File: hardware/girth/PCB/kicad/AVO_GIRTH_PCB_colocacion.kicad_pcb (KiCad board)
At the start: 4 copper layers, 65.5 x 43.5 mm, 115 parts, among them J1 USB-C 16P, J2 BATERÍA 1S, K1 G6KU-2F-Y DC3, Q1 AO3401A, Q10 AO3401A, Q11 AO3400A, Q12 2N7002, Q13 AO3400A, Q14 AO3401A, Q15 2N7002, Q16 2N7002, Q2 AO3401A, Q3 AO3401A, SW1 REED (1), SW2 REED (2), U1 BQ51013BRHLR, U2 BQ24072RGTR, U3 RT9080-33GJ5, U4 ESP32-C6-MINI-1U-N4, U5 BNO085, U6 USBLC6-2SC6, Y1 32,768 kHz 12,5 pF

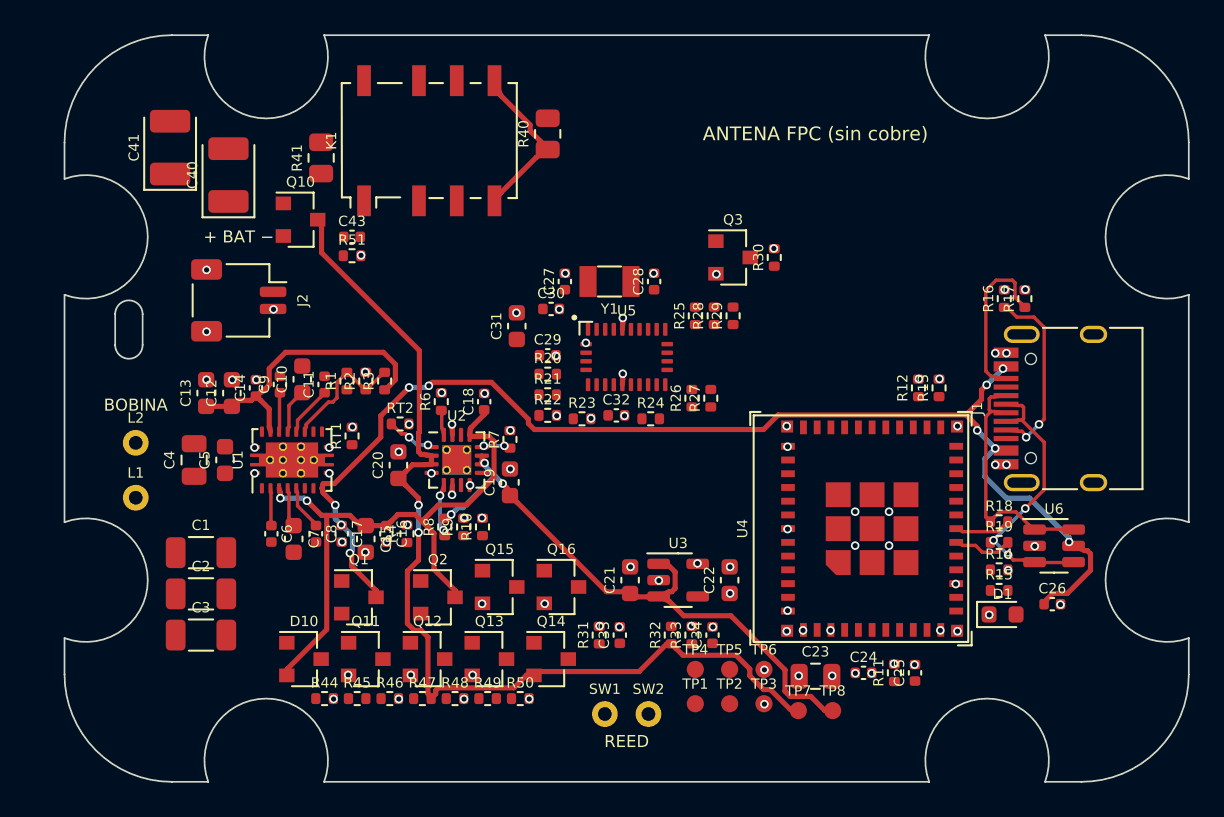
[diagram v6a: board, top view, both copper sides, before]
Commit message: PCB cincha: relé también se cierra desde el ESP32 (GPIO14), puerta de fabricación en CI, reparación de ruteado
- Relé: camino SET por firmware (Q17/Q18/D11/R52–R55): con la base puesta el ESP32 vive del camino de potencia del
  cargador y puede volver a cerrar el relé → el sistema nunca queda bloqueado apagado.
- GND de las QFN unidos a su pad térmico por pistas cortas (sin vías que tapen la salida de los pines vecinos).
- Referencias en la capa Fab; huellas enlazadas a los símbolos (DRC con paridad de esquema).
- CI: puerta bloqueante (0 errores DRC, 0 incompletas, 0 paridad, ERC limpio); ficheros FINAL solo si pasa; rojo si no.
- fuente/repair.py: completa las conexiones que deja Freerouting y genera la placa ruteada que usa el CI.

Co-Authored-By: Claude Opus 5.5 <noreply@anthropic.com>
Claude-Session: https://claude.ai/code/session_01CHDvF8BfHwPLkrFs9S3ECm
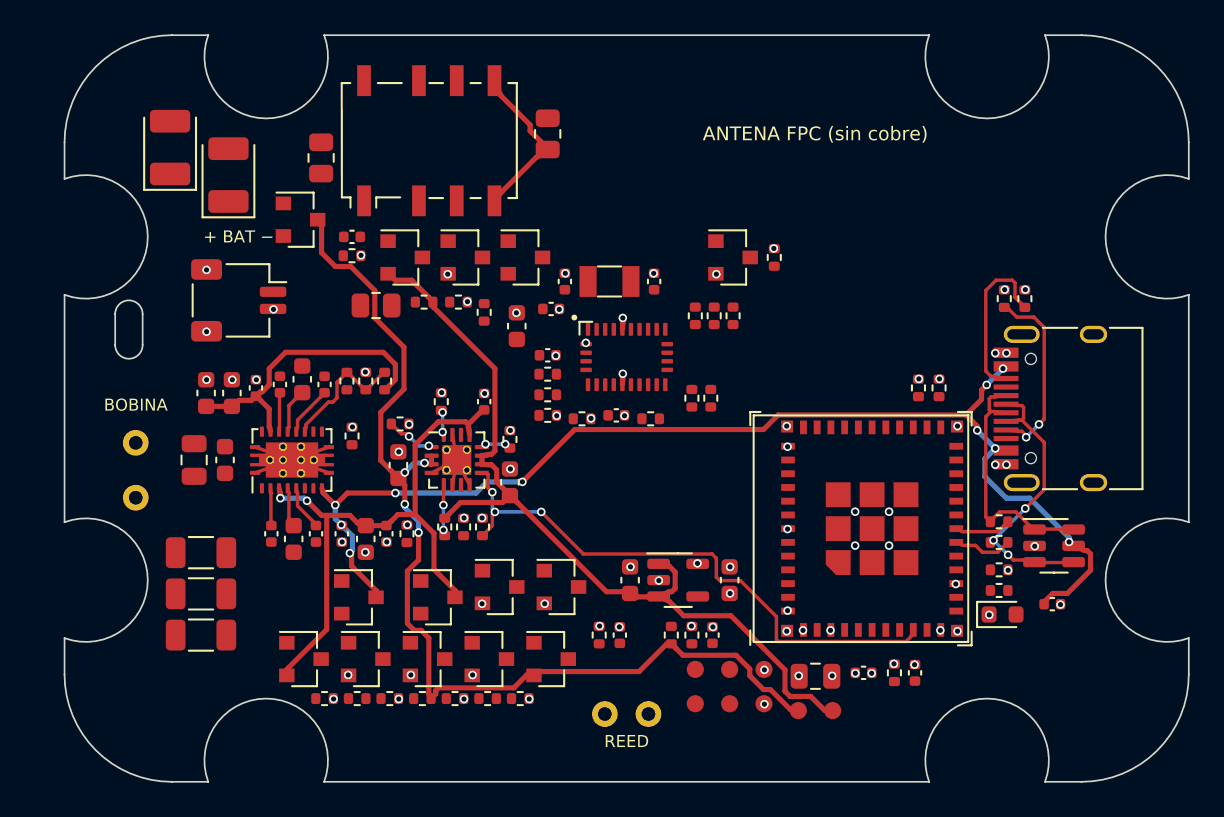
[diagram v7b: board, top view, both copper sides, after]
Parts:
- added D11: BAT54C, AVO:SOT-23, F.Cu at (94.1, 91.2)
- added Q17: AO3401A, AVO:SOT-23, F.Cu at (87.1, 91.2)
- added Q18: 2N7002, AVO:SOT-23, F.Cu at (90.6, 91.2)
- added R52: 10R, AVO:R_0805_2012Metric, F.Cu at (85.4, 94.0)
- added R53: 100k, AVO:R_0402_1005Metric, F.Cu at (88.2, 93.8)
- added R54: 100k, AVO:R_0402_1005Metric, F.Cu at (90.2, 93.8)
- added R55: 1k, AVO:R_0402_1005Metric, F.Cu at (91.7, 94.4)
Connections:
- U4 pad 19: (no net) -> RLY_ON
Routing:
- net CHG_STAT: track 0.00 -> 33.8 mm, vias 0 -> 3
- net VSYS: track 34.8 -> 49.7 mm, vias 3 -> 0
- net GND: track 5.87 -> 10.6 mm, vias 80 -> 74
- net VBUS: track 72.7 -> 69.1 mm
- net VBAT: track 58.6 -> 60.4 mm, vias 2 -> 4
- net VIN5: track 36.1 -> 35.0 mm
- net CHG_ISET: track 1.45 -> 1.47 mm, vias 0 -> 2

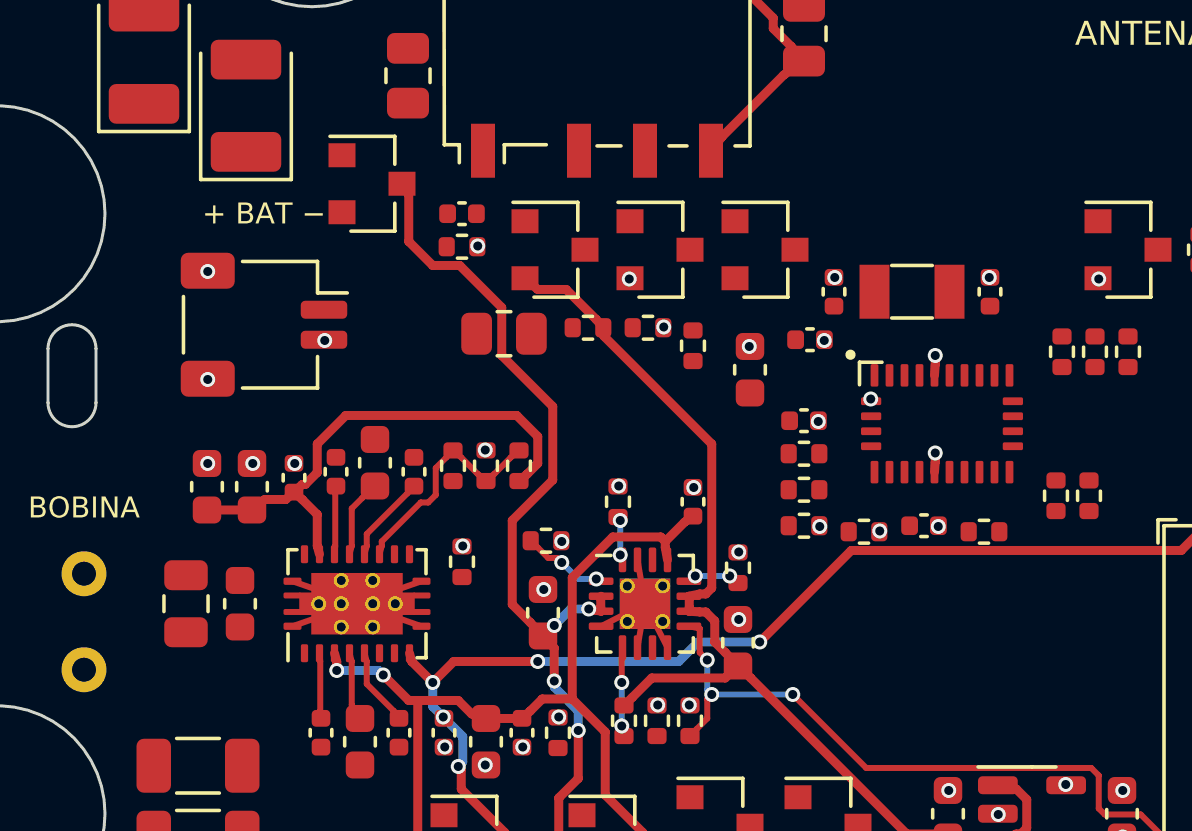
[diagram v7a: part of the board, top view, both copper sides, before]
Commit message: PCB cincha: etiquetas globales (paridad esquema-placa), puentes rectos a los pads térmicos, serigrafía
Co-Authored-By: Claude Opus 5.5 <noreply@anthropic.com>
Claude-Session: https://claude.ai/code/session_01CHDvF8BfHwPLkrFs9S3ECm
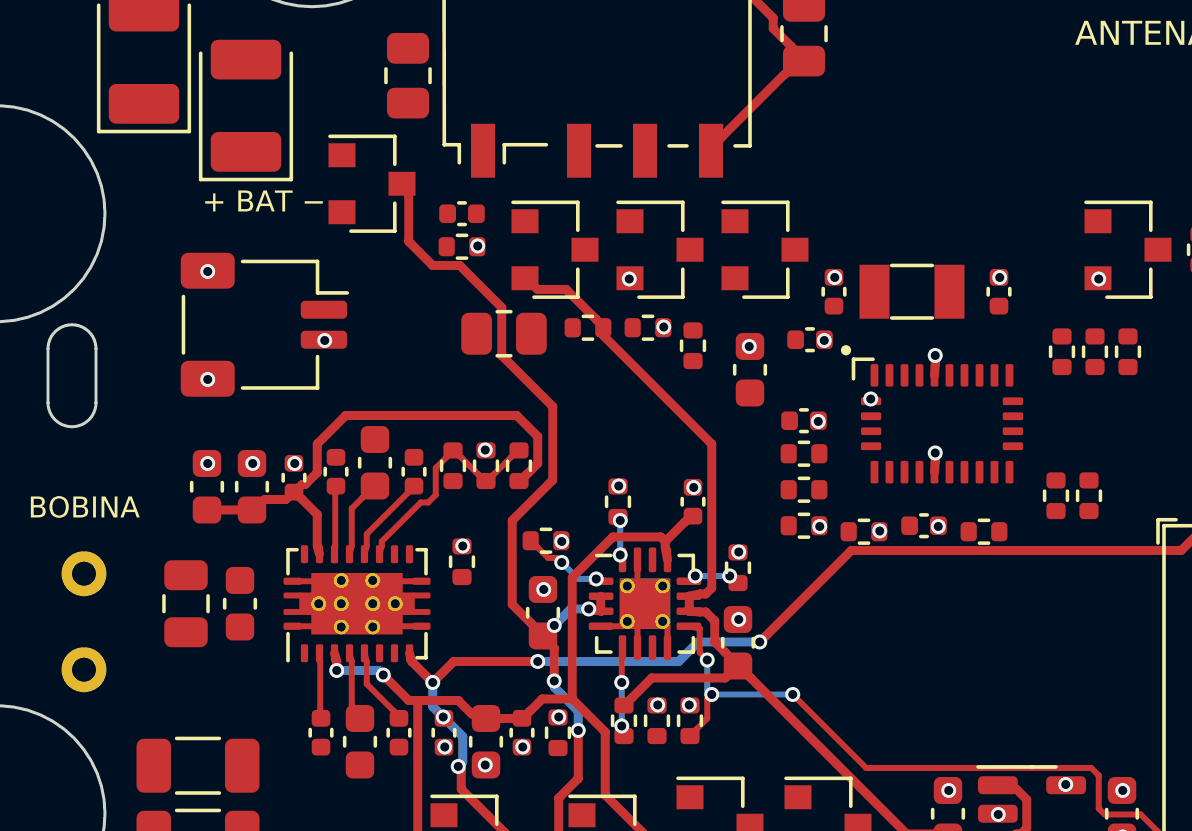
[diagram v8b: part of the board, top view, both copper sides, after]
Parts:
- moved C28 0.30 mm to (101.9, 92.6)
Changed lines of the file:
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@@
 		)
 		(fp_line
-			(start -2.75 -2.05)
-			(end -2 -2.05)
+			(start -2.95 -2.15)
+			(end -2.3 -2.15)
 			(stroke (width 0.12) (type solid))
 			(layer "F.SilkS")
 		)
 		(fp_line
-			(start -2.75 -2.05)
-			(end -2.75 -1.3)
+			(start -2.95 -2.15)
+			(end -2.95 -1.5)
 			(stroke (width 0.12) (type solid))
 			(layer "F.SilkS")
 		)
 		(fp_circle
-			(center -3.05 -2.3)
-			(end -2.93 -2.3)
+			(center -3.2 -2.45)
+			(end -3.08 -2.45)
 			(stroke (width 0.1) (type solid))
 			(fill solid)
@@
 		"AVO:C_0402_1005Metric"
 		(layer "F.Cu")
-		(at 101.6 92.6 90)
+		(at 101.9 92.6 90)
 		(descr
 			"Capacitor SMD 0402 (1005 Metric), square (rectangular) end terminal, IPC_7351 nominal, (Body size source: IPC-SM-782 page 76, https://www.pcb-3d.com/wordpress/wp-content/uploads/ipc-sm-782a_amendment_1_and_2.pdf), generated with kicad-footprint-generator"
@@
 	(segment
 		(start 78.35 102.25)
-		(end 79.0582 102.497)
+		(end 79.1 102.25)
 		(width 0.2)
 		(layer "F.Cu")
@@
 	(segment
 		(start 82.65 102.25)
-		(end 81.9418 102.497)
+		(end 81.9 102.25)
 		(width 0.2)
 		(layer "F.Cu")
@@
 	(segment
 		(start 82.65 103.75)
-		(end 81.9418 103.503)
+		(end 81.9 103.75)
 		(width 0.2)
 		(layer "F.Cu")
@@
 	(segment
 		(start 78.35 103.75)
-		(end 79.0582 103.503)
+		(end 79.1 103.75)
 		(width 0.2)
 		(layer "F.Cu")
@@
 	(segment
 		(start 88.6375 103.75)
-		(end 89.3049 103.4078)
+		(end 89.3875 103.75)
 		(width 0.2)
 		(layer "F.Cu")
@@
 	(segment
 		(start 89.85 104.4625)
-		(end 89.9764 103.7232)
+		(end 89.85 103.7125)
 		(width 0.2)
 		(layer "F.Cu")
@@
 	(segment
 		(start 90.85 104.4625)
-		(end 90.5078 103.7951)
+		(end 90.85 103.7125)
 		(width 0.2)
 		(layer "F.Cu")
@@
 	(segment
 		(start 89.85 101.5375)
-		(end 89.9764 102.2768)
+		(end 89.85 102.2875)
 		(width 0.2)
 		(layer "F.Cu")
@@
 	)
 	(segment
-		(start 101.6 92.12)
-		(end 101.575 92.125)
+		(start 101.9 92.12)
+		(end 101.925 92.125)
 		(width 0.3)
 		(layer "F.Cu")
@@
 	)
 	(via
-		(at 101.575 92.125)
+		(at 101.925 92.125)
 		(size 0.5)
 		(drill 0.3)
@@
 	(gr_text
 		"+ BAT −"
-		(at 77.4 90)
+		(at 77.4 89.6)
 		(layer "F.SilkS")
 		(effects (font (size 0.7 0.7) (thickness 0.12)))
